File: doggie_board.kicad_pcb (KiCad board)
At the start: 2 copper layers, 127 x 127.5 mm, 128 parts, among them J1 Conn_01x02, J2 XT90PW-M, J3 XT90PW-M, J5V1 Conn_01x02, J5V10 Conn_01x02, J5V11 Conn_01x02, J5V12 Conn_01x02, J5V13 Conn_01x02, J5V14 Conn_01x02, J5V15 Conn_01x02, J5V16 Conn_01x02, J5V17 Conn_01x02, J5V18 Conn_01x02, J5V19 Conn_01x02, J5V2 Conn_01x02, J5V20 Conn_01x02, J5V21 Conn_01x02, J5V22 Conn_01x02, J5V23 Conn_01x02, J5V24 Conn_01x02, J5V3 Conn_01x02, J5V4 Conn_01x02, J5V5 Conn_01x02, J5V6 Conn_01x02, J5V7 Conn_01x02, J5V8 Conn_01x02, J5V9 Conn_01x02, Q1 PSMN3R7-100BSEJ, Q2 PSMN3R7-100BSEJ, Q3 PSMN3R7-100BSEJ, Q4 PSMN3R7-100BSEJ, Q5 PSMN3R7-100BSEJ, Q6 PSMN3R7-100BSEJ, U1 TPS2490, U2 LM5148RGYR, U3 TPS566242DRLR, U4 TPS566242DRLR, U5 LM76005

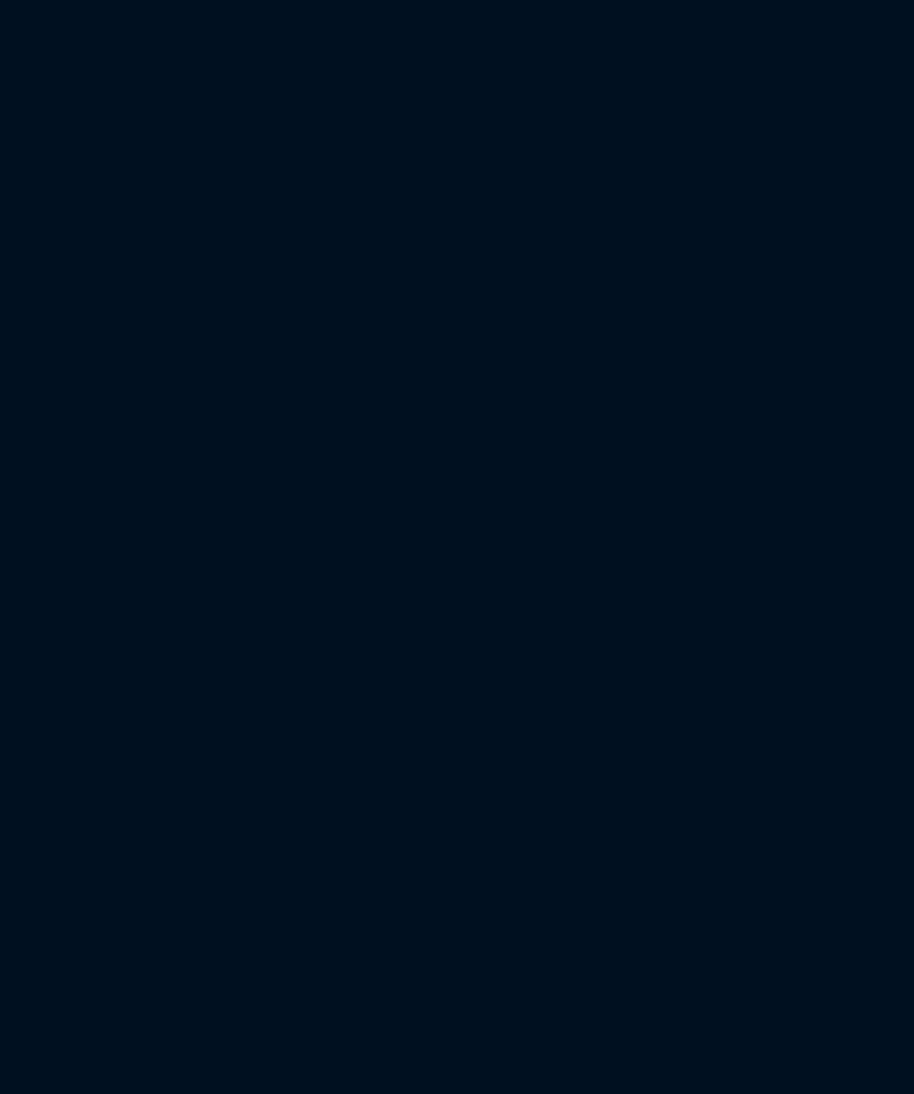
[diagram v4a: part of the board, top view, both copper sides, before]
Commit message: added footprints and standardized EN headers
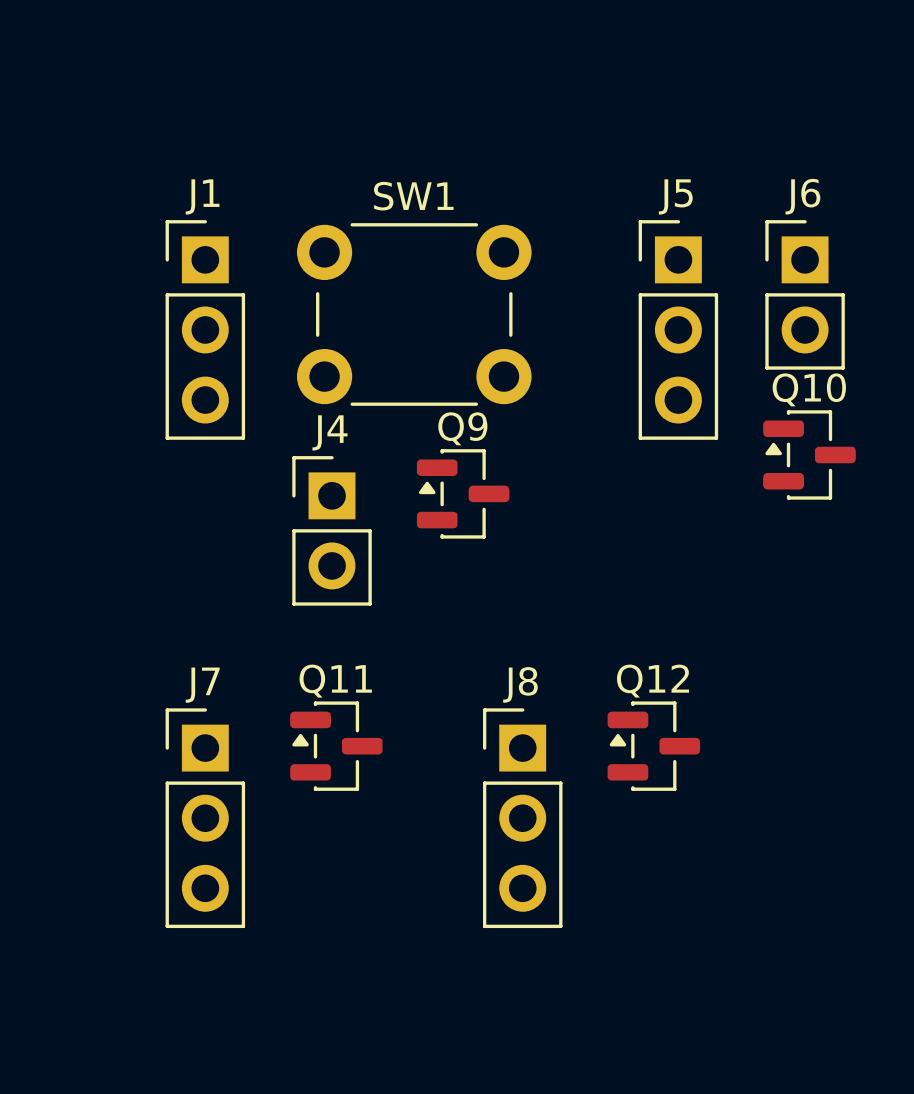
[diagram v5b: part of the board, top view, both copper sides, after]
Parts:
- added J1: Conn_01x03, Connector_PinHeader_2.54mm:PinHeader_1x03_P2.54mm_Vertical, F.Cu at (250.0, 86.2)
- added J4: Conn_01x02, Connector_PinHeader_2.54mm:PinHeader_1x02_P2.54mm_Vertical, F.Cu at (254.6, 94.8)
- added J5: Conn_01x03, Connector_PinHeader_2.54mm:PinHeader_1x03_P2.54mm_Vertical, F.Cu at (267.1, 86.2)
- added J6: Conn_01x02, Connector_PinHeader_2.54mm:PinHeader_1x02_P2.54mm_Vertical, F.Cu at (271.7, 86.2)
- added J7: Conn_01x03, Connector_PinHeader_2.54mm:PinHeader_1x03_P2.54mm_Vertical, F.Cu at (250.0, 103.9)
- added J8: Conn_01x03, Connector_PinHeader_2.54mm:PinHeader_1x03_P2.54mm_Vertical, F.Cu at (261.5, 103.9)
- added Q10: 2N7002, Package_TO_SOT_SMD:SOT-23, F.Cu at (271.9, 93.3)
- added Q11: 2N7002, Package_TO_SOT_SMD:SOT-23, F.Cu at (254.8, 103.8)
- added Q12: 2N7002, Package_TO_SOT_SMD:SOT-23, F.Cu at (266.2, 103.8)
- added Q9: 2N7002, Package_TO_SOT_SMD:SOT-23, F.Cu at (259.3, 94.7)
- added SW1: SW_SPST, Button_Switch_THT:SW_PUSH_6mm, F.Cu at (254.3, 86.0)
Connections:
- net /12v Buck Converter/PFM_SYNC renamed /12v Buck Converter/VDDA
- R19 pad 2: /5v Buck Converter/EN -> +5V_LP
- R20 pad 1: /5v Buck Converter/EN -> +5V_LP
- U2 pad 17: Net-(U2-PG/SYNCOUT) -> 12V_PG
- U2 pad 19: 48_RAW -> /12v Buck Converter/12V_EN
- U3 pad 5: /5v Buck Converter/EN -> Net-(Q11-S)
- U4 pad 5: /3.3v Buck Converter/EN -> Net-(Q12-S)

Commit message: pcb routing
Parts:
- removed Cboot1, Cboot2, Cboot3: 470nF, 20mOhm, Capacitor_SMD:C_0805_2012Metric_Pad1.18x1.45mm_HandSolder
- removed Cin1, Cin2: 4.7uF, 5.89mOhm, Capacitor_SMD:C_0805_2012Metric_Pad1.18x1.45mm_HandSolder
- removed Cinx1, Cinx2, Cinx3: 470nF, 33.996mOhm, Capacitor_SMD:C_0805_2012Metric_Pad1.18x1.45mm_HandSolder
- removed Cout1, Cout2: 150uF, Capacitor_SMD:C_0805_2012Metric_Pad1.18x1.45mm_HandSolder
- removed Cout3: 220uF, 10 mOhm, Capacitor_SMD:C_0805_2012Metric_Pad1.18x1.45mm_HandSolder
- removed Coutx1: 470nF, 87.491mOhm, Capacitor_SMD:C_0805_2012Metric_Pad1.18x1.45mm_HandSolder
- removed Coutx2: 470nF, 57.491mOhm, Capacitor_SMD:C_0805_2012Metric_Pad1.18x1.45mm_HandSolder
- removed Coutx3: 470nF, 58.782mOhm, Capacitor_SMD:C_0805_2012Metric_Pad1.18x1.45mm_HandSolder
- removed Ct2: 1nF, Capacitor_SMD:C_0805_2012Metric_Pad1.18x1.45mm_HandSolder
- removed Cvcc1, Cvcc2: 2.2uF, 7.674mOhm, Capacitor_SMD:C_0805_2012Metric_Pad1.18x1.45mm_HandSolder
- removed Cvcc3: 2.2uF, 7.474mOhm, Capacitor_SMD:C_0805_2012Metric_Pad1.18x1.45mm_HandSolder
- removed the J1 at (236.1, 32.3)
- removed the J1 at (250.0, 86.2)
- removed L1: 4.7u, Inductor_SMD:L_6.3x6.3_H3
- removed L1(2)1: 4.7uH, 13.1mOhm, Inductor_SMD:L_6.3x6.3_H3
- removed R23: 100k, Resistor_SMD:R_0201_0603Metric_Pad0.64x0.40mm_HandSolder
- removed R24: 20k, Resistor_SMD:R_0201_0603Metric_Pad0.64x0.40mm_HandSolder
- removed Rfbb1: 9.09k, Resistor_SMD:R_0201_0603Metric
- removed Rfbb2: 24.9k, Resistor_SMD:R_0201_0603Metric
- removed Rfbb3: 43.2k, Resistor_SMD:R_0201_0603Metric
- removed Rfbt1, Rfbt2, Rfbt3, Rpgood1, Rpgood2, Rpgood3: 100k, Resistor_SMD:R_0201_0603Metric
- removed U5: LM76005, Package_DFN_QFN:Texas_RNP0030B_WQFN-30-1EP_4x6mm_P0.5mm_EP1.8x4.5mm
- added J1: Conn_01x03, Connector_PinHeader_2.54mm:PinHeader_1x03_P2.54mm_Vertical, F.Cu at (139.2, 158.1)
- added R18: 6m 1W, Resistor_SMD:R_1206_3216Metric_Pad1.30x1.75mm_HandSolder, F.Cu at (126.8, 112.6)
- D1, D2: value 15KPA048C-SD-Q -> 5.0SMDJ58A; footprint footprints:DIODE_15KPA048C-SD-Q_BRN -> Diode_SMD:D_SMB-SMC_Universal_Handsoldering
- H1, H2, H3, H4: footprint MountingHole:MountingHole_5.3mm_M5_DIN965_Pad_TopBottom -> MountingHole:MountingHole_3.2mm_M3_DIN965_Pad_TopBottom
- J5V1, J5V10, J5V11, J5V12, J5V2, J5V3, J5V4, J5V5, J5V6, J5V7, J5V8, J5V9: value Conn_01x02 -> 48v
- J5V13: value Conn_01x02 -> 12v
- J5V14, J5V15, J5V16: value Conn_01x02 -> 12v; footprint Connector_PinHeader_1.00mm:PinHeader_1x02_P1.00mm_Vertical -> Connector_PinHeader_2.54mm:PinHeader_1x02_P2.54mm_Vertical
- J5V17, J5V18, J5V19, J5V20: value Conn_01x02 -> 3.3v; footprint Connector_PinHeader_1.00mm:PinHeader_1x02_P1.00mm_Vertical -> Connector_PinHeader_2.54mm:PinHeader_1x02_P2.54mm_Vertical
- J5V21: value Conn_01x02 -> 5v
- J5V22, J5V23, J5V24: value Conn_01x02 -> 5v; footprint Connector_PinHeader_1.00mm:PinHeader_1x02_P1.00mm_Vertical -> Connector_PinHeader_2.54mm:PinHeader_1x02_P2.54mm_Vertical
- R1: value 212k -> 300k
- R15: value 100k -> 470k
- moved C10 221.6 mm to (51.6, 158.4), turned to 90 degrees
- moved C11 220.0 mm to (52.4, 158.4), turned to 90 degrees
- moved C12 218.5 mm to (53.2, 158.4), turned to 90 degrees
- moved C20 218.2 mm to (49.0, 158.4), turned to 90 degrees
- moved C19 217.5 mm to (50.6, 158.4), turned to 90 degrees
- moved C21 216.7 mm to (49.8, 158.4), turned to 90 degrees
- moved H4 211.5 mm to (43.4, 161.0)
- moved H3 193.6 mm to (44.8, 43.8)
- moved C18 189.6 mm to (87.8, 157.4), turned to 90 degrees
- moved C17 188.9 mm to (90.0, 157.8), turned to 90 degrees
- moved C14 188.3 mm to (85.6, 157.8), turned to 90 degrees
- moved J5V15 188.3 mm to (54.1, 161.2)
- moved C16 187.6 mm to (92.6, 157.8), turned to 90 degrees
- moved C15 186.8 mm to (94.8, 157.8), turned to 90 degrees
- moved C24 178.6 mm to (98.1, 158.6)
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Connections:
- D2 pad 1: 48_L -> 48_RAW
- R15 pad 1: /12v Buck Converter/VCC -> +12V
- R15 pad 2: Net-(U2-PG/SYNCOUT) -> 12V_PG
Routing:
- net ps_sw: track 0.00 -> 6.50 mm
- net Net-(Q9-S): track 0.00 -> 6.50 mm
- net Net-(Q1-Pad1): track 0.00 -> 4.45 mm
- net Net-(Q3-Pad1): track 0.00 -> 4.26 mm
- net Net-(Q2-Pad1): track 0.00 -> 4.21 mm
- net Net-(Q4-Pad1): track 0.00 -> 4.19 mm
- net Net-(Q6-Pad1): track 0.00 -> 3.77 mm
- net Net-(Q5-Pad1): track 0.00 -> 3.77 mm
- added copper zone on F.Cu, net /High Side Power Switch/drain_line
- added copper zone on F.Cu, net 48_RAW
- added copper zone on B.Cu, net GND
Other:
- board size 127 x 127.5 mm -> 127 x 127 mm
- copper layers 2 -> 4

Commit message: additional progress on routing front copper
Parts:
- moved SW1 117.9 mm to (147.3, 158.3)
- moved Q9 110.5 mm to (138.9, 154.0)
- moved C9 88.0 mm to (53.8, 158.4), turned to 90 degrees
- moved R17 57.7 mm to (91.0, 156.0)
- moved R18 47.9 mm to (79.0, 115.0)
- moved U2 46.4 mm to (84.8, 113.9)
- moved Q10 45.8 mm to (125.4, 147.6), turned to -90 degrees
- moved R15 45.5 mm to (80.0, 113.0)
- moved R5 41.7 mm to (104.6, 71.2)
- moved C8 40.8 mm to (86.0, 109.0)
- moved C5 40.7 mm to (88.0, 131.0)
- moved U4 39.9 mm to (88.0, 152.0)
- moved U1 35.8 mm to (122.8, 108.2)
- moved R19 35.5 mm to (112.0, 156.0)
- moved R13 34.5 mm to (87.0, 118.0)
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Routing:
- net ps_sw: track 6.50 -> 0.00 mm
- net Net-(Q9-S): track 6.50 -> 0.00 mm
- net Net-(Q1-Pad1): track 4.45 -> 0.00 mm
- net Net-(Q3-Pad1): track 4.26 -> 0.00 mm
- net Net-(Q2-Pad1): track 4.21 -> 0.00 mm
- net Net-(Q4-Pad1): track 4.19 -> 0.00 mm
- net Net-(Q6-Pad1): track 3.77 -> 0.00 mm
- net Net-(Q5-Pad1): track 3.77 -> 0.00 mm

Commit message: march 14
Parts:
- moved C4 42.7 mm to (106.9, 145.4), turned to -90 degrees
- moved R15 42.4 mm to (108.8, 144.1), turned to -90 degrees
- moved R18 41.2 mm to (110.5, 141.5)
- moved C8 38.2 mm to (97.8, 145.3), turned to 180 degrees
- moved C6 35.0 mm to (96.0, 143.6), turned to 90 degrees
- moved U2 34.9 mm to (103.9, 143.2), turned to 0 degrees
- moved R16 31.3 mm to (100.4, 143.6), turned to 90 degrees
- moved U1 28.8 mm to (102.7, 128.8), turned to 180 degrees
- moved Ct1 25.9 mm to (108.2, 128.8), turned to 90 degrees
- moved C7 25.7 mm to (97.4, 143.5), turned to -90 degrees
- moved R4 25.6 mm to (109.5, 128.8), turned to 90 degrees
- moved R13 24.4 mm to (95.1, 141.0), turned to -90 degrees
- moved R3 23.0 mm to (107.2, 128.6), turned to 90 degrees
- moved R14 22.7 mm to (93.0, 140.9), turned to -90 degrees
- moved Q11 16.3 mm to (108.7, 156.3)
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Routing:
- net /High Side Power Switch/gate_line: track 0.00 -> 103.2 mm
- net GND: track 0.00 -> 39.5 mm
- net +12V: track 0.00 -> 36.5 mm
- net +5V_LP: track 0.00 -> 30.8 mm
- net /5v Buck Converter/5V_EN: track 0.00 -> 25.5 mm
- net /12v Buck Converter/12V_EN: track 0.00 -> 24.6 mm, vias 0 -> 1
- net 12V_PG: track 0.00 -> 22.8 mm
- net +5V: track 0.00 -> 22.3 mm
- net Net-(J6-Pin_1): track 0.00 -> 22.0 mm
- net /3.3v Buck Converter/3V3_EN: track 0.00 -> 19.1 mm
- net Net-(Q6-Pad1): track 0.00 -> 16.0 mm
- net Net-(Q9-S): track 0.00 -> 12.3 mm
- net Net-(U2-CNFG): track 0.00 -> 10.6 mm
- net Net-(Q12-S): track 0.00 -> 10.3 mm
- net /12v Buck Converter/RT: track 0.00 -> 8.60 mm
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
